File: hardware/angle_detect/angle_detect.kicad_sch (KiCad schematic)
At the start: 31 parts, among them J1 MPU_1, J2 MPU_2, J3 USB_C_Receptacle_USB2.0, J4 IIC_OLED, J5 SWD, SW1 NRST_BUTTON, U1 STM32G474RETx, U3 AMS1117-3.3, U3 CP2102N-Axx-xQFN28, Y1 24MHz

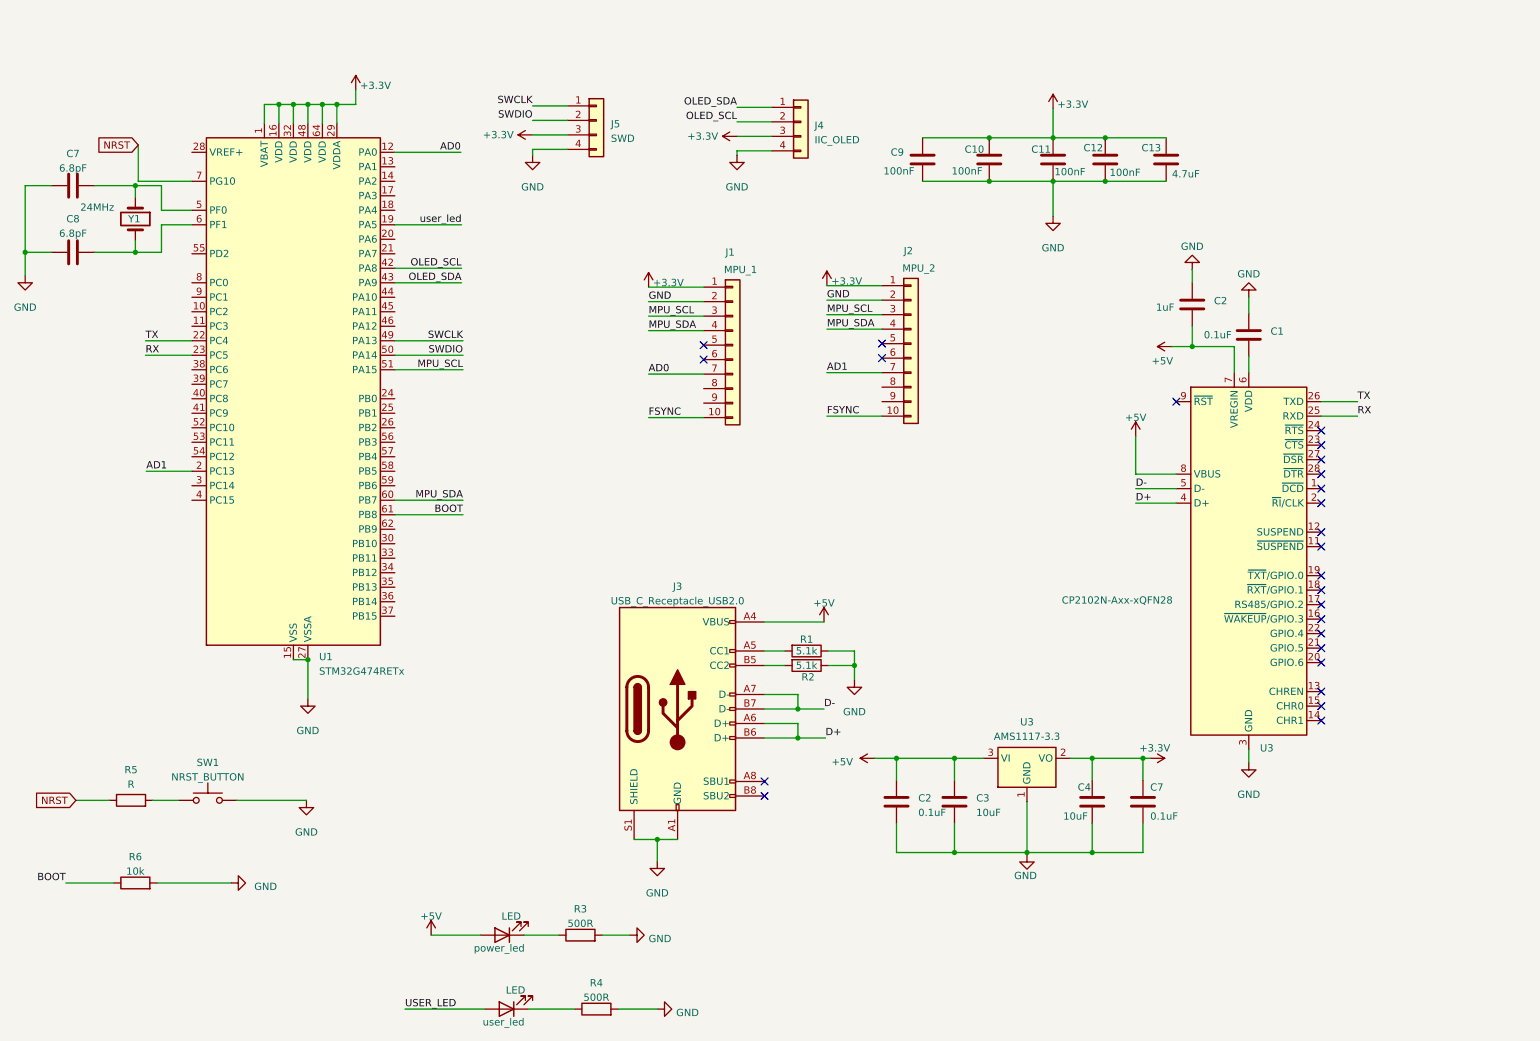
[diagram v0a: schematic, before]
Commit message: freertos init
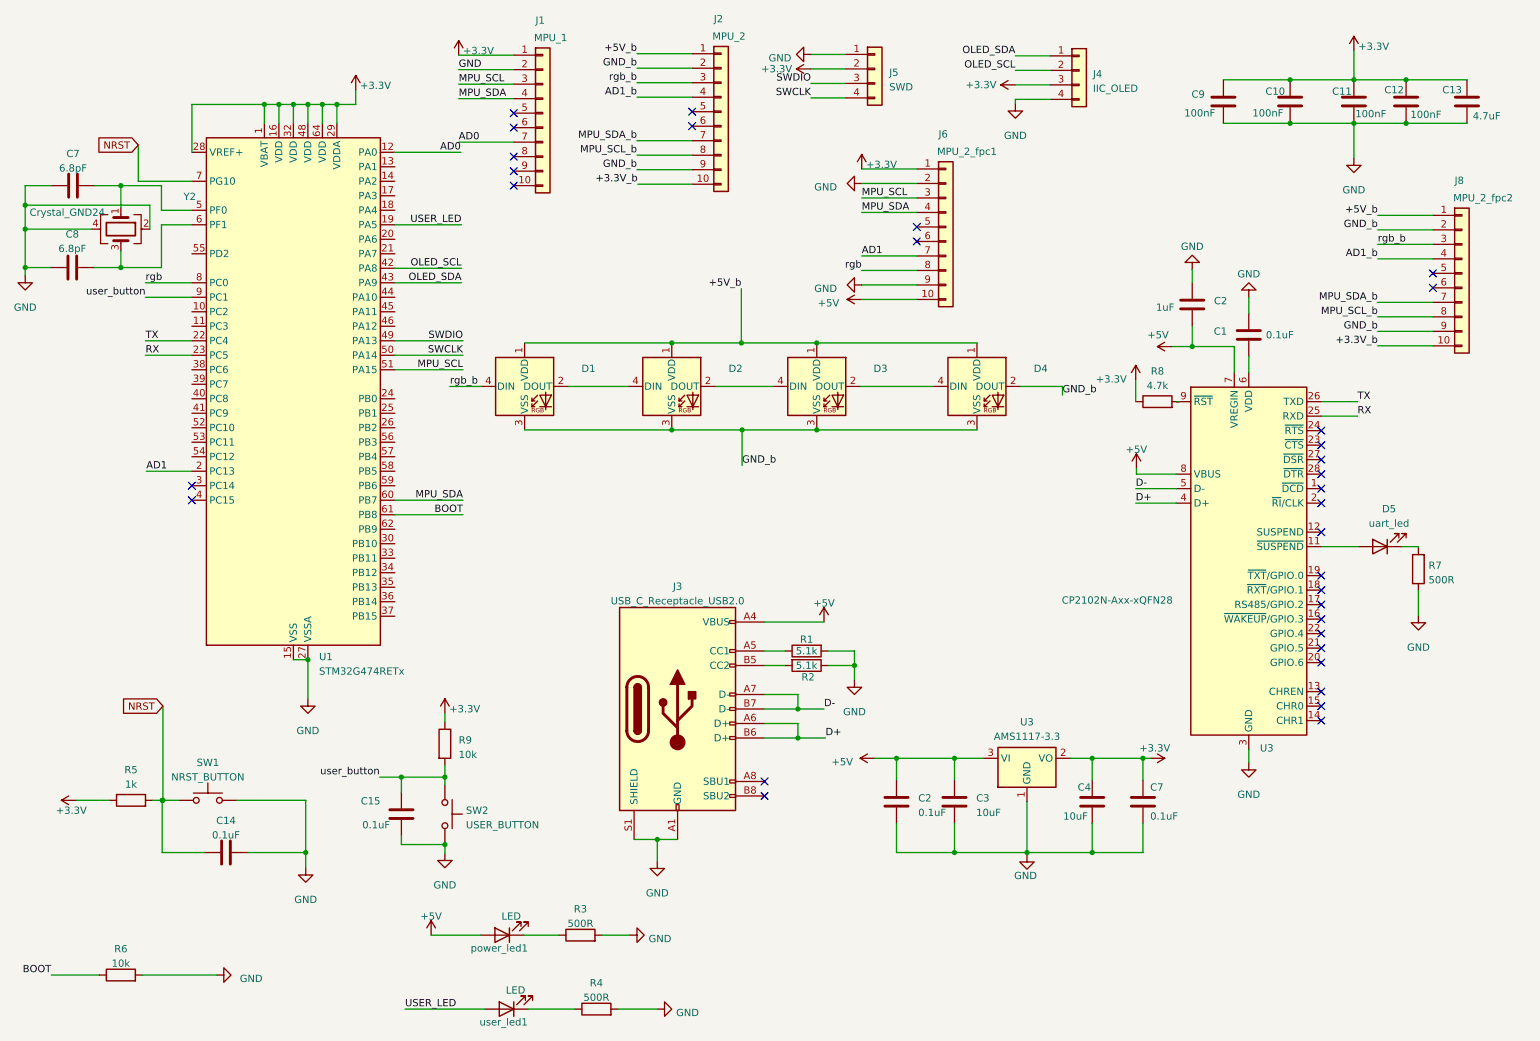
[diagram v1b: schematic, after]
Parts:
- removed Y1: 24MHz, symbol Device:Crystal
- added C14, C15: 0.1uF, Capacitor_SMD:C_0603_1608Metric_Pad1.08x0.95mm_HandSolder, symbol Device:C
- added D1, D2, D3, D4: WS2812B, LED_SMD:LED_WS2812B_PLCC4_5.0x5.0mm_P3.2mm, symbol LED:WS2812B
- added D5: uart_led, LED_SMD:LED_0603_1608Metric_Pad1.05x0.95mm_HandSolder, symbol Device:LED
- added J6: MPU_2_fpc1, Connector_FFC-FPC:TE_1-1734839-0_1x10-1MP_P0.5mm_Horizontal, symbol Connector_Generic:Conn_01x10
- added J8: MPU_2_fpc2, Connector_FFC-FPC:TE_1-1734839-0_1x10-1MP_P0.5mm_Horizontal, symbol Connector_Generic:Conn_01x10
- added R7: 500R, Resistor_SMD:R_0603_1608Metric_Pad0.98x0.95mm_HandSolder, symbol Device:R
- added R8: 4.7k, Resistor_SMD:R_0603_1608Metric_Pad0.98x0.95mm_HandSolder, symbol Device:R
- added R9: 10k, Resistor_SMD:R_0603_1608Metric_Pad0.98x0.95mm_HandSolder, symbol Device:R
- added SW2: USER_BUTTON, Button_Switch_SMD:SW_SPST_B3U-1000P, symbol Switch:SW_Push
- added Y2: Crystal_GND24, Crystal:Crystal_SMD_2016-4Pin_2.0x1.6mm, symbol Device:Crystal_GND24
- C1, C10, C11, C12, C13, C2, C7, C8, C9: footprint (none) -> Capacitor_SMD:C_0603_1608Metric_Pad1.08x0.95mm_HandSolder
- J1, J2: footprint (none) -> Connector_PinSocket_2.54mm:PinSocket_1x10_P2.54mm_Vertical
- J3: footprint (none) -> Connector_USB:USB_C_Receptacle_G-Switch_GT-USB-7010ASV
- J4: footprint (none) -> Connector_PinSocket_2.54mm:PinSocket_1x04_P2.54mm_Vertical
- J5: footprint (none) -> Connector_PinHeader_2.54mm:PinHeader_1x04_P2.54mm_Horizontal
- R1, R2, R3, R4, R6: footprint (none) -> Resistor_SMD:R_0603_1608Metric_Pad0.98x0.95mm_HandSolder
- R5: value R -> 1k; footprint (none) -> Resistor_SMD:R_0603_1608Metric_Pad0.98x0.95mm_HandSolder
- SW1: footprint (none) -> Button_Switch_SMD:SW_SPST_B3U-1000P
- power_led1: renamed from power_led; footprint (none) -> LED_SMD:LED_0603_1608Metric
- user_led1: renamed from user_led; footprint (none) -> Capacitor_SMD:C_0603_1608Metric_Pad1.08x0.95mm_HandSolder
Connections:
- net user_led is gone; now on net USER_LED: U1.19 (PA5)
- net +3.3V: now also J5.2 (Pin_2), R5.1, U1.28 (VREF+), J6.1 (Pin_1), R8.1, R9.1; no longer J2.1 (Pin_1), J5.3 (Pin_3)
- net +5V: now also J6.10 (Pin_10)
- net AD1: now also J6.7 (Pin_7); no longer J2.7 (Pin_7)
- net GND: now also J5.1 (Pin_1), R1.2, C14.2, C15.1, J6.2 (Pin_2), J6.9 (Pin_9), R7.1, SW2.2, Y2.2, Y2.4; no longer J2.2 (Pin_2), J5.4 (Pin_4), R1.1
- net MPU_SCL: now also J6.3 (Pin_3); no longer J2.3 (Pin_3)
- net MPU_SDA: now also J6.4 (Pin_4); no longer J2.4 (Pin_4)
- net NRST: now also R5.2, SW1.1, C14.1; no longer R5.1
- net SWCLK: now also J5.4 (Pin_4), U1.50 (PA14); no longer J5.1 (Pin_1), U1.49 (PA13)
- net SWDIO: now also J5.3 (Pin_3), U1.49 (PA13); no longer J5.2 (Pin_2), U1.50 (PA14)
- net at C7.2, U1.5 (PF0): now also Y2.1
- net at C8.2, U1.6 (PF1): now also Y2.3
- net at J3.A5 (CC1): now also R1.1; no longer R1.2
- net at U3.11 (~{SUSPEND}): now also D5.2 (A)
- net at U3.9 (~{RST}): now also R8.2
- net MPU_SCL_b: now reaches J2.8 (Pin_8)
- net MPU_SCL_b: now also J8.8 (Pin_8)
- net GND_b: now reaches J2.9 (Pin_9)
- net GND_b: now also J2.2 (Pin_2), D1.3 (VSS), D2.3 (VSS), D3.3 (VSS), D4.2 (DOUT), D4.3 (VSS), J8.2 (Pin_2), J8.9 (Pin_9)
- net rgb: now reaches U1.8 (PC0)
- net rgb: now also J6.8 (Pin_8)
- net user_button: now reaches U1.9 (PC1)
- net user_button: now also C15.2, R9.2, SW2.1
- net FSYNC: no longer names the net of J1.10 (Pin_10)
- net FSYNC: no longer J2.10 (Pin_10)
- new net: D2.2 (DOUT), D3.4 (DIN)
- new net: D1.2 (DOUT), D2.4 (DIN)
- new net: D3.2 (DOUT), D4.4 (DIN)
- new net: D5.1 (K), R7.2
- new net +3.3V_b: J2.10 (Pin_10), J8.10 (Pin_10)
- new net +5V_b: D1.1 (VDD), D2.1 (VDD), D3.1 (VDD), D4.1 (VDD), J2.1 (Pin_1), J8.1 (Pin_1)
- new net AD1_b: J2.4 (Pin_4), J8.4 (Pin_4)
- new net MPU_SDA_b: J2.7 (Pin_7), J8.7 (Pin_7)
- new net rgb_b: D1.4 (DIN), J2.3 (Pin_3), J8.3 (Pin_3)
- no-connect marks 25 -> 32
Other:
- moved on the sheet: C10, C11, C12, C13, C8, C9, J1, J2, J4, J5, R1, R6
